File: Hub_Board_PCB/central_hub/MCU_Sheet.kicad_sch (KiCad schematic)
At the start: 67 parts, among them J1 CX90B-16P, J2 Barrel_Jack_Switch, J3 TSM-105-01-S-DV-M-TR, J4 Screw_Terminal_01x08, J5 PH2-06-UA, J6 Screw_Terminal_01x04, J7 Screw_Terminal_01x14, SW1 RotaryEncoder_Switch, SW2 SW_Push, U1 R7FA4M1AB3CFM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

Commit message: - added global net-labels and reorganized pages - 4.0" TFT SPI 480*320 V2.1 display may already have a level-shifter (actually has HR2046, touch screen controller) so may not need to include voltage dividers and NMOSes
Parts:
- removed C11: 4.7nF, symbol Device:C
- removed C12, C13, C16, C17: 22uF, symbol Device:C
- removed C14: 100nF, symbol Device:C
- removed C15: 10uF, symbol Device:C
- removed D1: PRTR5V0U2X,215, Package_TO_SOT_SMD:SOT-143, symbol Power_Protection:PRTR5V0U2X
- removed D2, D4: PMEG6020AELRX, Diode_SMD:Nexperia_CFP3_SOD-123W, symbol Diode:PMEG6020AELR
- removed J1: CX90B-16P, CON18_1X12_P0_HIR, symbol CX90B-16P:CX90B-16P
- removed J2: Barrel_Jack_Switch, symbol Connector:Barrel_Jack_Switch
- removed J3: TSM-105-01-S-DV-M-TR, CONN_TSM-105-01-S-DV-M-TR_SAI, symbol TSM-105-01-S-DV-M-TR:TSM-105-01-S-DV-M-TR
- removed J4: Screw_Terminal_01x08, symbol Connector:Screw_Terminal_01x08
- removed J5: PH2-06-UA, CONN_PH2-06-UA_ADM, symbol PH2-06-UA:PH2-06-UA
- removed J6: Screw_Terminal_01x04, symbol Connector:Screw_Terminal_01x04
- removed J7: Screw_Terminal_01x14, symbol Connector:Screw_Terminal_01x14
- removed L3: 4.7uH, symbol Device:L
- removed R9: 1M, symbol Device:R
- removed SW1: RotaryEncoder_Switch, symbol Device:RotaryEncoder_Switch
- removed TP2, TP3, TP4, TP5, TP6: TestPoint, symbol Connector:TestPoint
- removed U2: AP63205WU-7, SOIC_05WU-7_DIO, symbol AP63205WU-7:AP63205WU-7
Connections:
- net +3.3V: no longer C6.2, C9.2, U1.20 (VCC_USB), U1.4 (VBATT)
- net P000_AN00_AMP+ renamed A1
- net P001_AN01_AMP- renamed A2
- net P002_AN02_AMPO renamed A3
- net P014_AN09_DAC renamed A0
- net P102_SPI0_RSPCK_GPT2_B_CAN0_RX renamed D5
- net P103_SPI0_SSL_GPT2_A_CAN0_TX renamed D4
- net P104_IRQ01_GPT1_B renamed D3
- net P105_IRQ00_GPT1_A renamed D2
- net P106_GPT0_B renamed D6
- net P107_GPT0_A renamed D7
- net P108_SWDIO renamed P108
- net P109_SCI9_TXD renamed D11
- net P110_SCI9_RXD renamed D12
- net P111_GPT3_A renamed D13
- net P112_GPT3_B renamed D10
- net P300_SWCLK renamed P300
- net P301_SCI2_RXD renamed D0
- net P302_SCI2_TXD renamed D1
- net P303_GPT7_B renamed D9
- net P304_GPT7_A renamed D8
- net P501_SCI1_TXD renamed P501
- net P502_SCI1_RXD renamed P502
- net SCL_Accel renamed A5
- net SDA_Accel renamed A4
- net USB_D_N renamed USB_D-
- net USB_D_P renamed USB_D+
- new net MCU_3V3: C6.2, C9.2, U1.20 (VCC_USB), U1.4 (VBATT)
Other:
- note removed: "ANALOG HEADER"
- note removed: "BUCK CONVERTER"
- note removed: "CS"
- note removed: "DAC"
- note removed: "DC JACK"
- note removed: "DIGITAL HEADER"
- note removed: "ESD PROTECTION"
- note removed: "GPS HEADER"
- note removed: "ICSP HEADER"
- note removed: "MISO"
- note removed: "MOSI"
- note removed: "OPAMP OUT"
- note removed: "OPAMP+"
- note removed: "OPAMP-"
- note removed: "RX"
- note removed: "RX on GPS"
- note removed: "SCHOTTKY FOR REVERSE POLARITY PROTECTION"
- note removed: "SCHOTTKY FOR USB OVERVOLTAGE PROTECTION"
- note removed: "SCK"
- note removed: "SWD CONNECTOR"
- note removed: "TX"
- note removed: "TX on GPS"
- note removed: "USB CONNECTOR"
- note removed: "diff pair"
- moved on the sheet: D3, D5, D6, D7, R10, R11, R12, R13, R14, R15, R2, R3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

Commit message: Added footprints for almost all components
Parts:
- C1, C10, C2, C3, C4, C5, C6, C7, C8, C9: footprint (none) -> Capacitor_SMD:C_0603_1608Metric
- D3, D5, D6, D7: footprint (none) -> Diode_SMD:D_0603_1608Metric
- L1, L2: footprint IND_BLM18_0603_MUR -> ~ALL:IND_BLM18_0603_MUR
- R1, R10, R11, R12, R13, R14, R15, R16, R2, R3, R4, R5, R6, R7, R8: footprint (none) -> Resistor_SMD:R_0603_1608Metric
- SW2: footprint (none) -> Button_Switch_SMD:SW_Push_1P1T_NO_6x6mm_H9.5mm
- TP1, TP10, TP11, TP7, TP8, TP9, love: footprint (none) -> TestPoint:TestPoint_Pad_D1.0mm
- U1: footprint PLQP0064KB-C_REN -> ~ALL:PLQP0064KB-C_REN

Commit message: Added all other footprints... populated all components with NO errors or warnings :)
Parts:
- Y1: footprint (none) -> Crystal:Crystal_HC49-U_Vertical
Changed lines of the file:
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@@
       (effects (font (size 1.27 1.27)) (justify right))
     )
-    (property "Footprint" "" (at 92.71 41.91 0)
+    (property "Footprint" "Crystal:Crystal_HC49-U_Vertical" (at 92.71 41.91 0)
       (effects (font (size 1.27 1.27)) hide)
     )

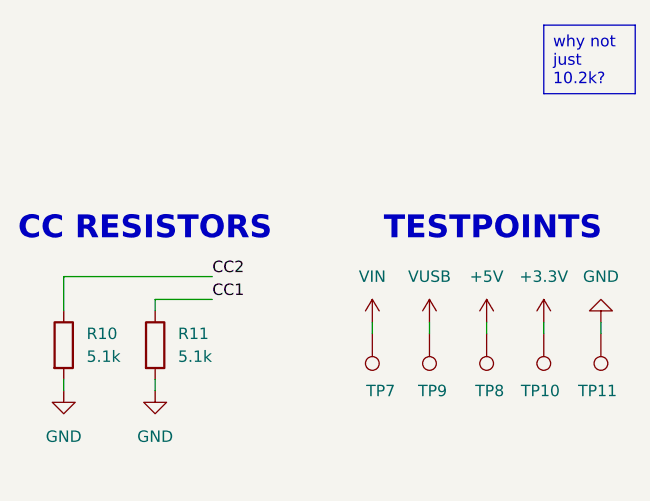
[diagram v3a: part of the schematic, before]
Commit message: Started Layout (hub board)
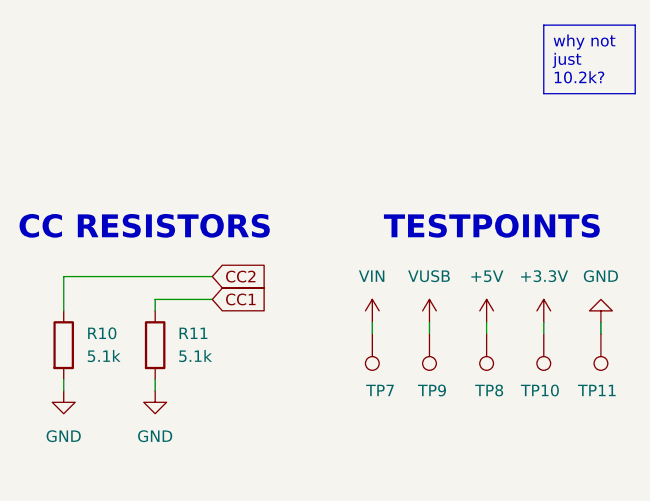
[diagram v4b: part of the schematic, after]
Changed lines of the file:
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@@
-    (effects (font (size 1.27 1.27)) (justify left bottom))
-  )
-  (label "CC1" (at 40.64 172.72 0) (fields_autoplaced)
     (effects (font (size 1.27 1.27)) (justify left bottom))
   )
@@
     (effects (font (size 1.27 1.27)) (justify left bottom))
   )
-  (label "CC2" (at 40.64 170.18 0) (fields_autoplaced)
-    (effects (font (size 1.27 1.27)) (justify left bottom))
-  )
   (label "P001_AN01_AMP-" (at 191.77 36.83 0) (fields_autoplaced)
     (effects (font (size 1.27 1.27)) (justify left bottom))
@@
     )
   )
+  (global_label "CC1" (shape input) (at 40.64 172.72 0) (fields_autoplaced)
+    (effects (font (size 1.27 1.27)) (justify left))
+    (property "Intersheetrefs" "${INTERSHEET_REFS}" (at 47.3521 172.72 0)
+      (effects (font (size 1.27 1.27)) (justify left) hide)
+    )
+  )
   (global_label "D4" (shape input) (at 228.6 69.85 0) (fields_autoplaced)
     (effects (font (size 1.27 1.27)) (justify left))
@@
       (effects (font (size 1.27 1.27)) (justify left) hide)
     )
+  )
+  (global_label "CC2" (shape input) (at 40.64 170.18 0) (fields_autoplaced)
+    (effects (font (size 1.27 1.27)) (justify left))
+    (property "Intersheetrefs" "${INTERSHEET_REFS}" (at 47.3521 170.18 0)
+      (effects (font (size 1.27 1.27)) (justify left) hide)
+    )

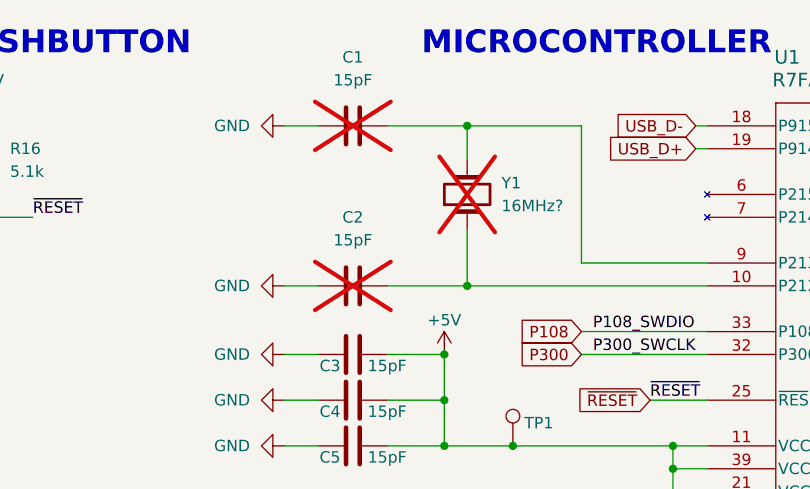
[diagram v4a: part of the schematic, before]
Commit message: Redid traces... might want auto trace lol
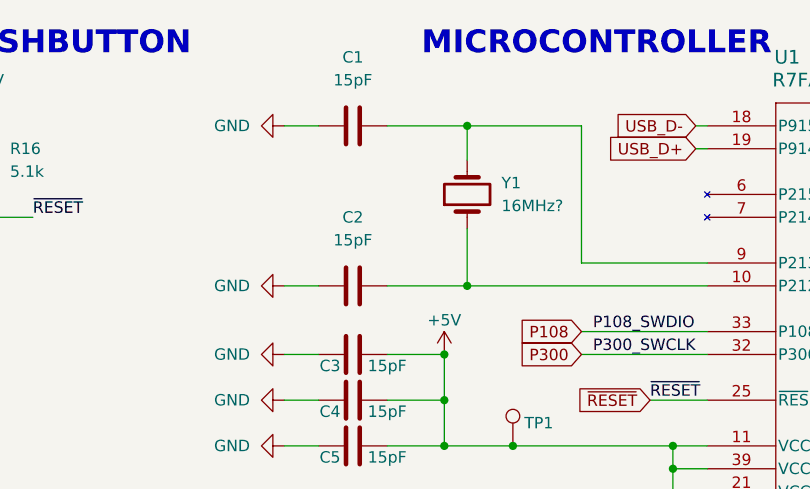
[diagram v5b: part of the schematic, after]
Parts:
- C1, C2, Y1: now fitted
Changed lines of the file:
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@@
   )
   (symbol (lib_id "Device:C") (at 80.01 34.29 90) (unit 1)
-    (in_bom yes) (on_board yes) (dnp yes) (fields_autoplaced)
+    (in_bom yes) (on_board yes) (dnp no) (fields_autoplaced)
     (property "Reference" "C1" (at 80.01 26.67 90)
       (effects (font (size 1.27 1.27)))
@@
   )
   (symbol (lib_id "Device:Crystal") (at 92.71 41.91 90) (unit 1)
-    (in_bom yes) (on_board yes) (dnp yes) (fields_autoplaced)
+    (in_bom yes) (on_board yes) (dnp no) (fields_autoplaced)
     (property "Reference" "Y1" (at 96.52 40.64 90)
       (effects (font (size 1.27 1.27)) (justify right))
@@
   )
   (symbol (lib_id "Device:C") (at 80.01 52.07 90) (unit 1)
-    (in_bom yes) (on_board yes) (dnp yes) (fields_autoplaced)
+    (in_bom yes) (on_board yes) (dnp no) (fields_autoplaced)
     (property "Reference" "C2" (at 80.01 44.45 90)
       (effects (font (size 1.27 1.27)))

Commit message: Meeting Changes
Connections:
- net MD renamed BOOT
- net P108: no longer names the net of U1.33 (P108/GTIOC0B/TMS/SWDIO)
- net P300: no longer names the net of U1.32 (P300/GTIOC0A/TCK/SWCLK)
- net P501: no longer names the net of U1.50 (GTIOC2B/AN017/P501)
- net P502: no longer names the net of U1.51 (GTIOC3B/AN018/P502)
- no-connect marks 0 -> 4
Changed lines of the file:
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@@
   (junction (at 82.55 85.09) (diameter 0) (color 0 0 0 0)
   )
+  (junction (at 233.68 102.87) (diameter 0) (color 0 0 0 0)
+  )
   (junction (at 73.66 87.63) (diameter 0) (color 0 0 0 0)
   )
@@
   (junction (at 256.54 128.27) (diameter 0) (color 0 0 0 0)
   )
+  (no_connect (at 119.38 57.15))
+  (no_connect (at 119.38 59.69))
+  (no_connect (at 190.5 133.35))
+  (no_connect (at 190.5 130.81))
   (wire (pts (xy 190.5 54.61) (xy 208.28 54.61))
     (stroke (width 0) (type default))
@@
     (stroke (width 0) (type default))
   )
-  (wire (pts (xy 105.41 59.69) (xy 119.38 59.69))
-    (stroke (width 0) (type default))
-  )
   (wire (pts (xy 91.44 133.35) (xy 91.44 132.08))
     (stroke (width 0) (type default))
@@
     (stroke (width 0) (type default))
   )
-  (wire (pts (xy 190.5 133.35) (xy 208.28 133.35))
-    (stroke (width 0) (type default))
-  )
   (wire (pts (xy 40.64 85.09) (xy 43.18 85.09))
     (stroke (width 0) (type default))
@@
     (stroke (width 0) (type default))
   )
-  (wire (pts (xy 190.5 130.81) (xy 208.28 130.81))
-    (stroke (width 0) (type default))
-  )
   (wire (pts (xy 90.17 64.77) (xy 90.17 69.85))
     (stroke (width 0) (type default))
@@
     (stroke (width 0) (type default))
   )
+  (wire (pts (xy 233.68 102.87) (xy 237.49 102.87))
+    (stroke (width 0) (type default))
+  )
   (wire (pts (xy 190.5 102.87) (xy 233.68 102.87))
     (stroke (width 0) (type default))
@@
   )
   (wire (pts (xy 73.66 96.52) (xy 73.66 97.79))
-    (stroke (width 0) (type default))
-  )
-  (wire (pts (xy 105.41 57.15) (xy 119.38 57.15))
     (stroke (width 0) (type default))
   )
@@
     (effects (font (size 1.27 1.27)) (justify left bottom))
   )
-  (label "P502_SCI1_RXD" (at 191.77 133.35 0) (fields_autoplaced)
-    (effects (font (size 1.27 1.27)) (justify left bottom))
-  )
   (label "~{RESET}" (at 113.03 64.77 0) (fields_autoplaced)
     (effects (font (size 1.27 1.27)) (justify left bottom))
@@
     (effects (font (size 1.27 1.27)) (justify left bottom))
   )
-  (label "P108_SWDIO" (at 106.68 57.15 0) (fields_autoplaced)
-    (effects (font (size 1.27 1.27)) (justify left bottom))
-  )
   (label "MD" (at 191.77 102.87 0) (fields_autoplaced)
     (effects (font (size 1.27 1.27)) (justify left bottom))
@@
     (effects (font (size 1.27 1.27)) (justify left bottom))
   )
-  (label "P501_SCI1_TXD" (at 191.77 130.81 0) (fields_autoplaced)
-    (effects (font (size 1.27 1.27)) (justify left bottom))
-  )
   (label "P110_SCI9_RXD" (at 191.77 87.63 0) (fields_autoplaced)
     (effects (font (size 1.27 1.27)) (justify left bottom))
@@
   )
   (label "P002_AN02_AMPO" (at 191.77 39.37 0) (fields_autoplaced)
-    (effects (font (size 1.27 1.27)) (justify left bottom))
-  )
-  (label "P300_SWCLK" (at 106.68 59.69 0) (fields_autoplaced)
     (effects (font (size 1.27 1.27)) (justify left bottom))
   )
@@
     )
   )
-  (global_label "P108" (shape input) (at 105.41 57.15 180) (fields_autoplaced)
-    (effects (font (size 1.27 1.27)) (justify right))
-    (property "Intersheetrefs" "${INTERSHEET_REFS}" (at 97.5263 57.15 0)
-      (effects (font (size 1.27 1.27)) (justify right) hide)
-    )
-  )
   (global_label "D7" (shape input) (at 228.6 80.01 0) (fields_autoplaced)
     (effects (font (size 1.27 1.27)) (justify left))
@@
     )
   )
-  (global_label "P501" (shape input) (at 208.28 130.81 0) (fields_autoplaced)
-    (effects (font (size 1.27 1.27)) (justify left))
-    (property "Intersheetrefs" "${INTERSHEET_REFS}" (at 216.1637 130.81 0)
-      (effects (font (size 1.27 1.27)) (justify left) hide)
-    )
-  )
   (global_label "D1" (shape input) (at 208.28 118.11 0) (fields_autoplaced)
     (effects (font (size 1.27 1.27)) (justify left))
@@
     )
   )
-  (global_label "P300" (shape input) (at 105.41 59.69 180) (fields_autoplaced)
-    (effects (font (size 1.27 1.27)) (justify right))
-    (property "Intersheetrefs" "${INTERSHEET_REFS}" (at 97.5263 59.69 0)
-      (effects (font (size 1.27 1.27)) (justify right) hide)
-    )
-  )
   (global_label "A3" (shape input) (at 210.82 39.37 0) (fields_autoplaced)
     (effects (font (size 1.27 1.27)) (justify left))
@@
     )
   )
-  (global_label "P502" (shape input) (at 208.28 133.35 0) (fields_autoplaced)
-    (effects (font (size 1.27 1.27)) (justify left))
-    (property "Intersheetrefs" "${INTERSHEET_REFS}" (at 216.1637 133.35 0)
-      (effects (font (size 1.27 1.27)) (justify left) hide)
-    )
-  )
   (global_label "D0" (shape input) (at 208.28 115.57 0) (fields_autoplaced)
     (effects (font (size 1.27 1.27)) (justify left))
@@
       (effects (font (size 1.27 1.27)) (justify left) hide)
     )
+  )
+  (global_label "BOOT" (shape input) (at 237.49 102.87 0) (fields_autoplaced)
+    (effects (font (size 1.27 1.27)) (justify left))
+    (property "Intersheetrefs" "${INTERSHEET_REFS}" (at 245.3738 102.87 0)
+      (effects (font (size 1.27 1.27)) (justify left) hide)
+    )

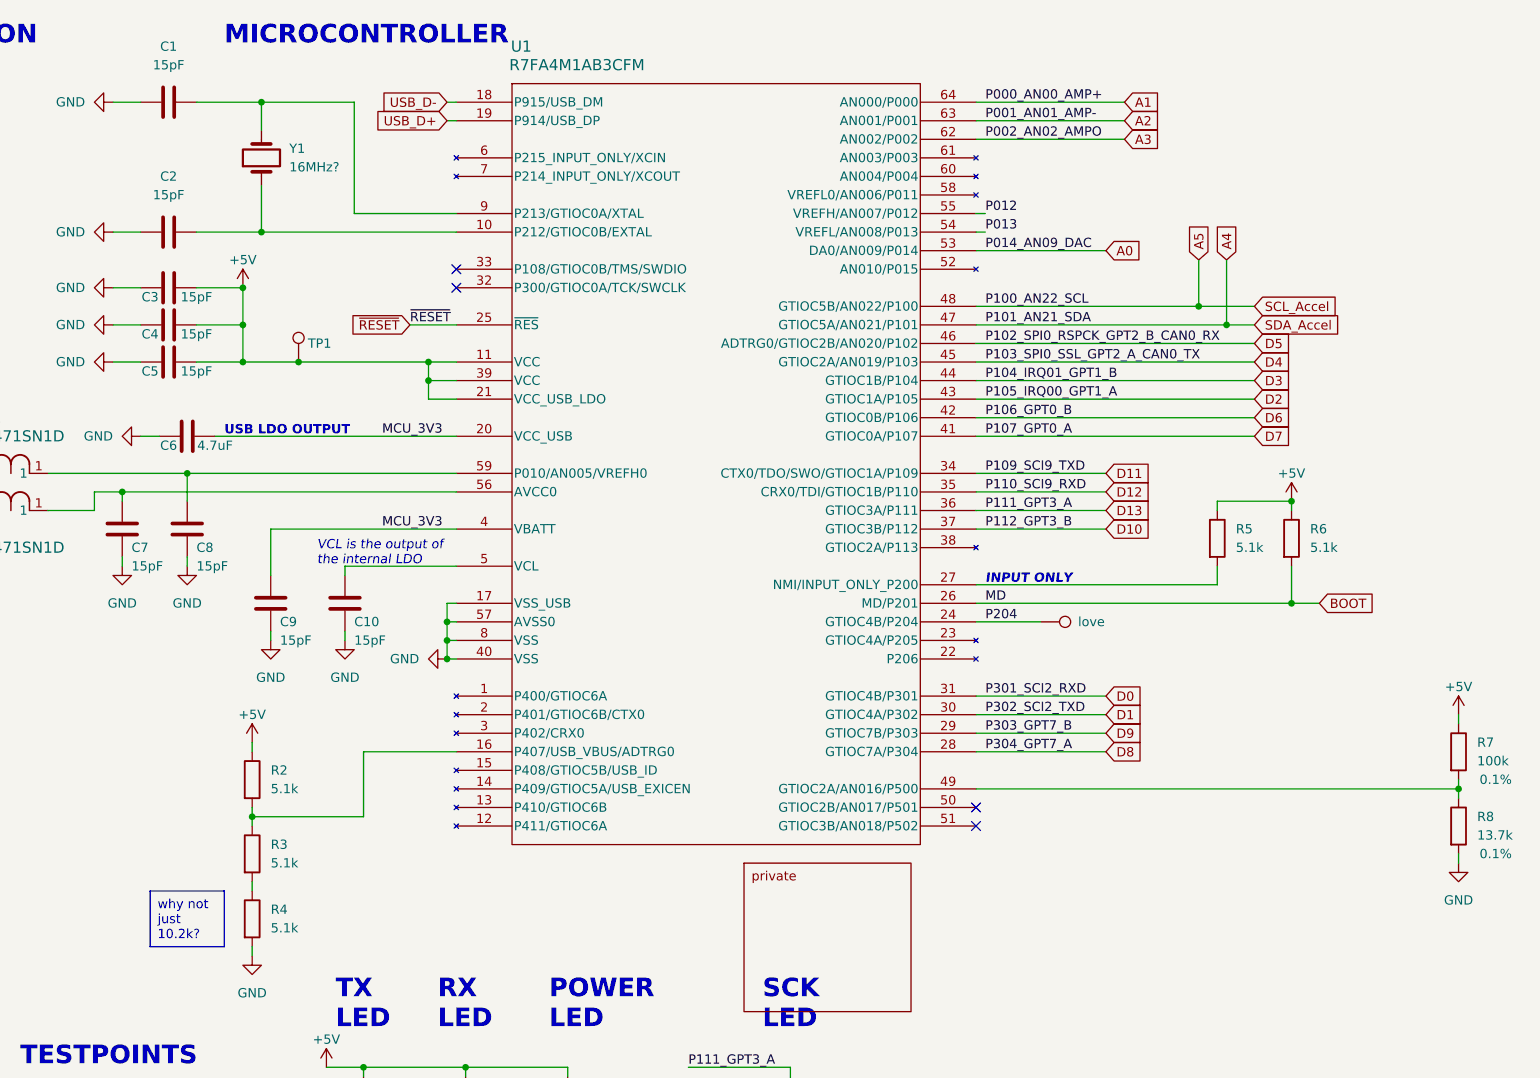
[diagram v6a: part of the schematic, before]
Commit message: - fixed capacitor values on MCU sheet (both central hub and motor board) - added missing Accelerometer componenets - changed BOOT HEADER (both central hub and motor board) - set the Arduino "love" signal to NC - fixed overlapping pins on USB connector
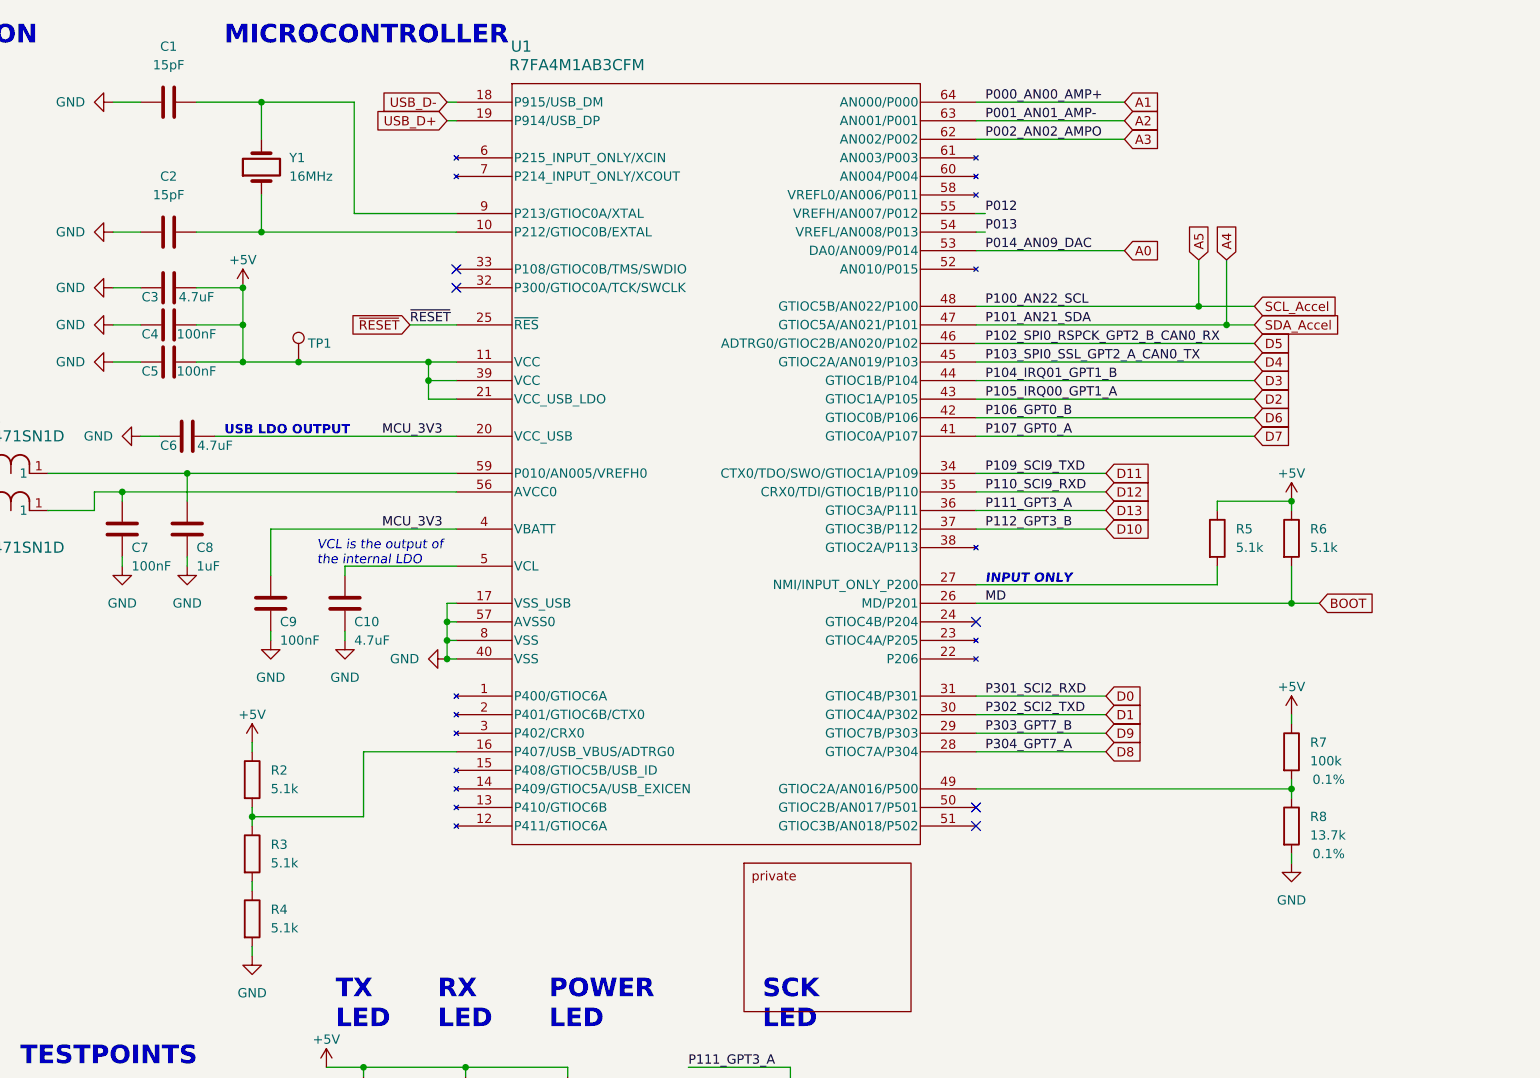
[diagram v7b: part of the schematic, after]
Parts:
- removed love: TestPoint, TestPoint:TestPoint_Pad_D1.0mm, symbol Connector:TestPoint
- C10, C3: value 15pF -> 4.7uF
- C4, C5, C7, C9: value 15pF -> 100nF
- C8: value 15pF -> 1uF
- Y1: value 16MHz? -> 16MHz
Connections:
- net P204: no longer names the net of U1.24 (GTIOC4B/P204)
- no-connect marks 4 -> 5
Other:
- moved on the sheet: R7, R8, Y1
